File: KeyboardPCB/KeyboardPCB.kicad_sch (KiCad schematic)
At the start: 2 parts

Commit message: Equipment added
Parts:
- gave numbers to parts that had none: 2
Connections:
- net MCU_Battery/VBUSOUT is gone; now on net +5V: P1.A4 (VBUS), P1.A9 (VBUS), P1.B4 (VBUS), P1.B9 (VBUS)
- net MCU_Battery/VBUSIN renamed +5V

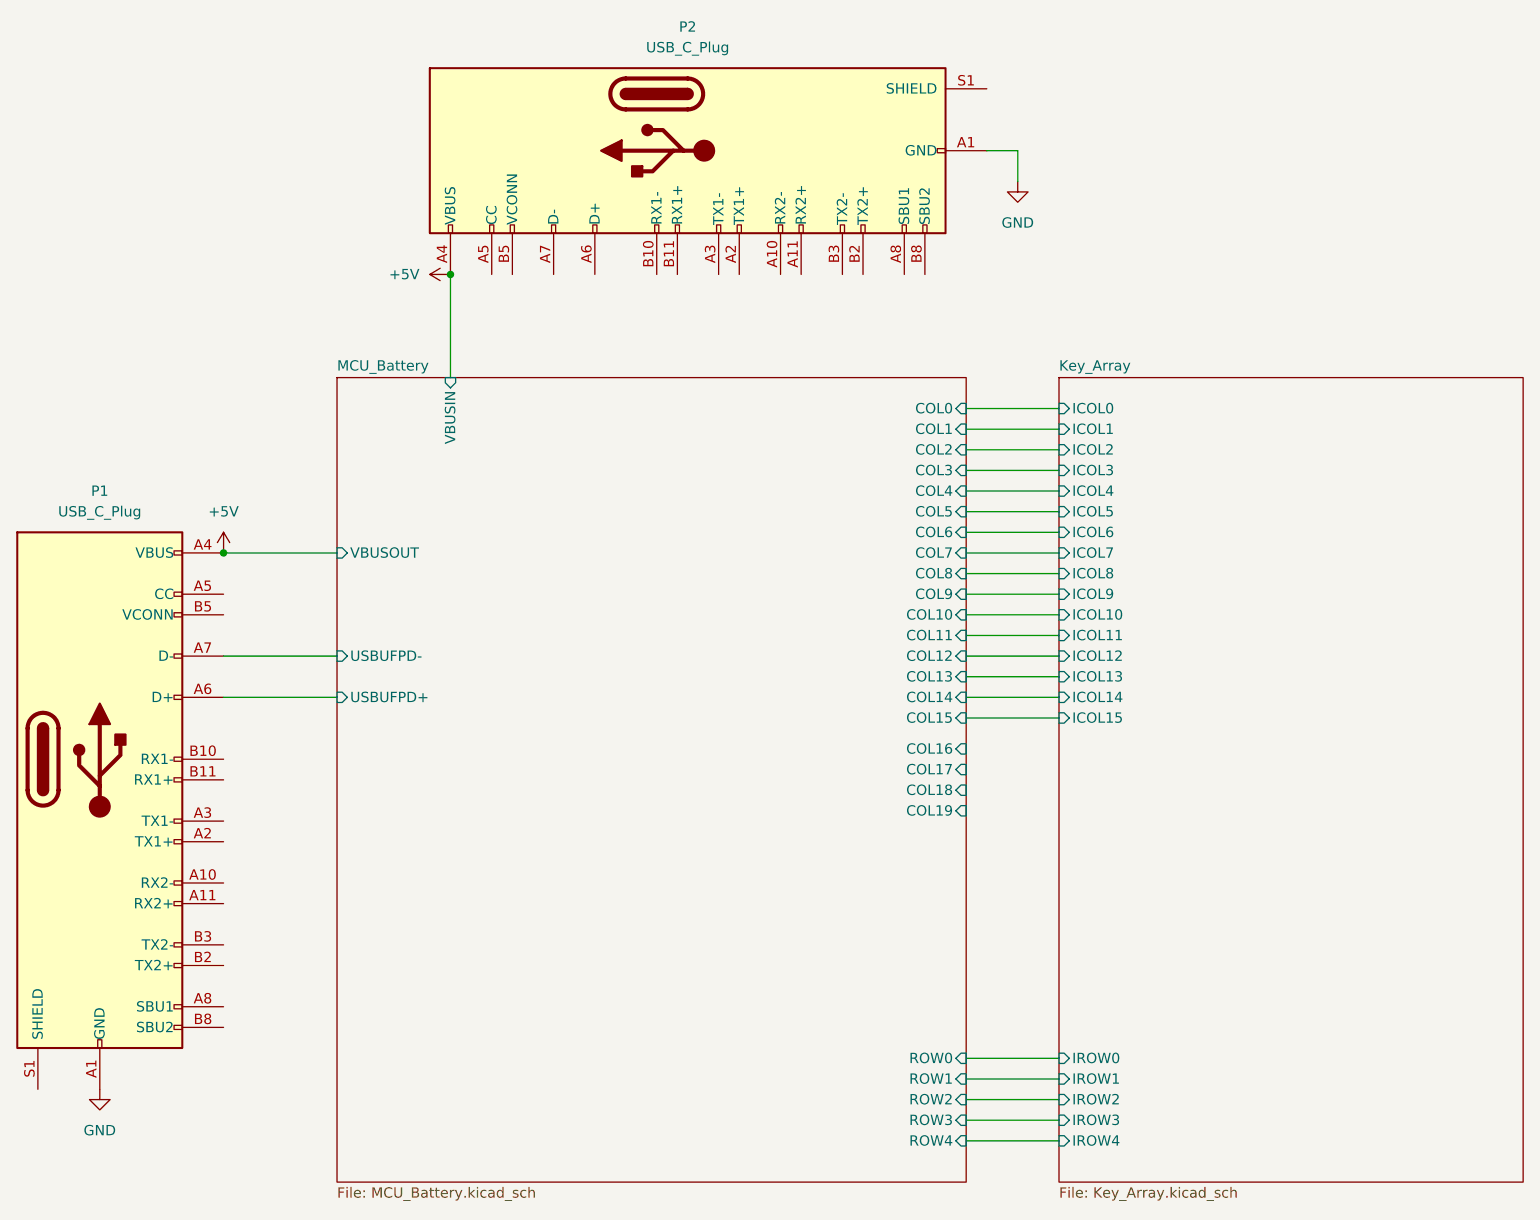
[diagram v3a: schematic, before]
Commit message: Added NCs
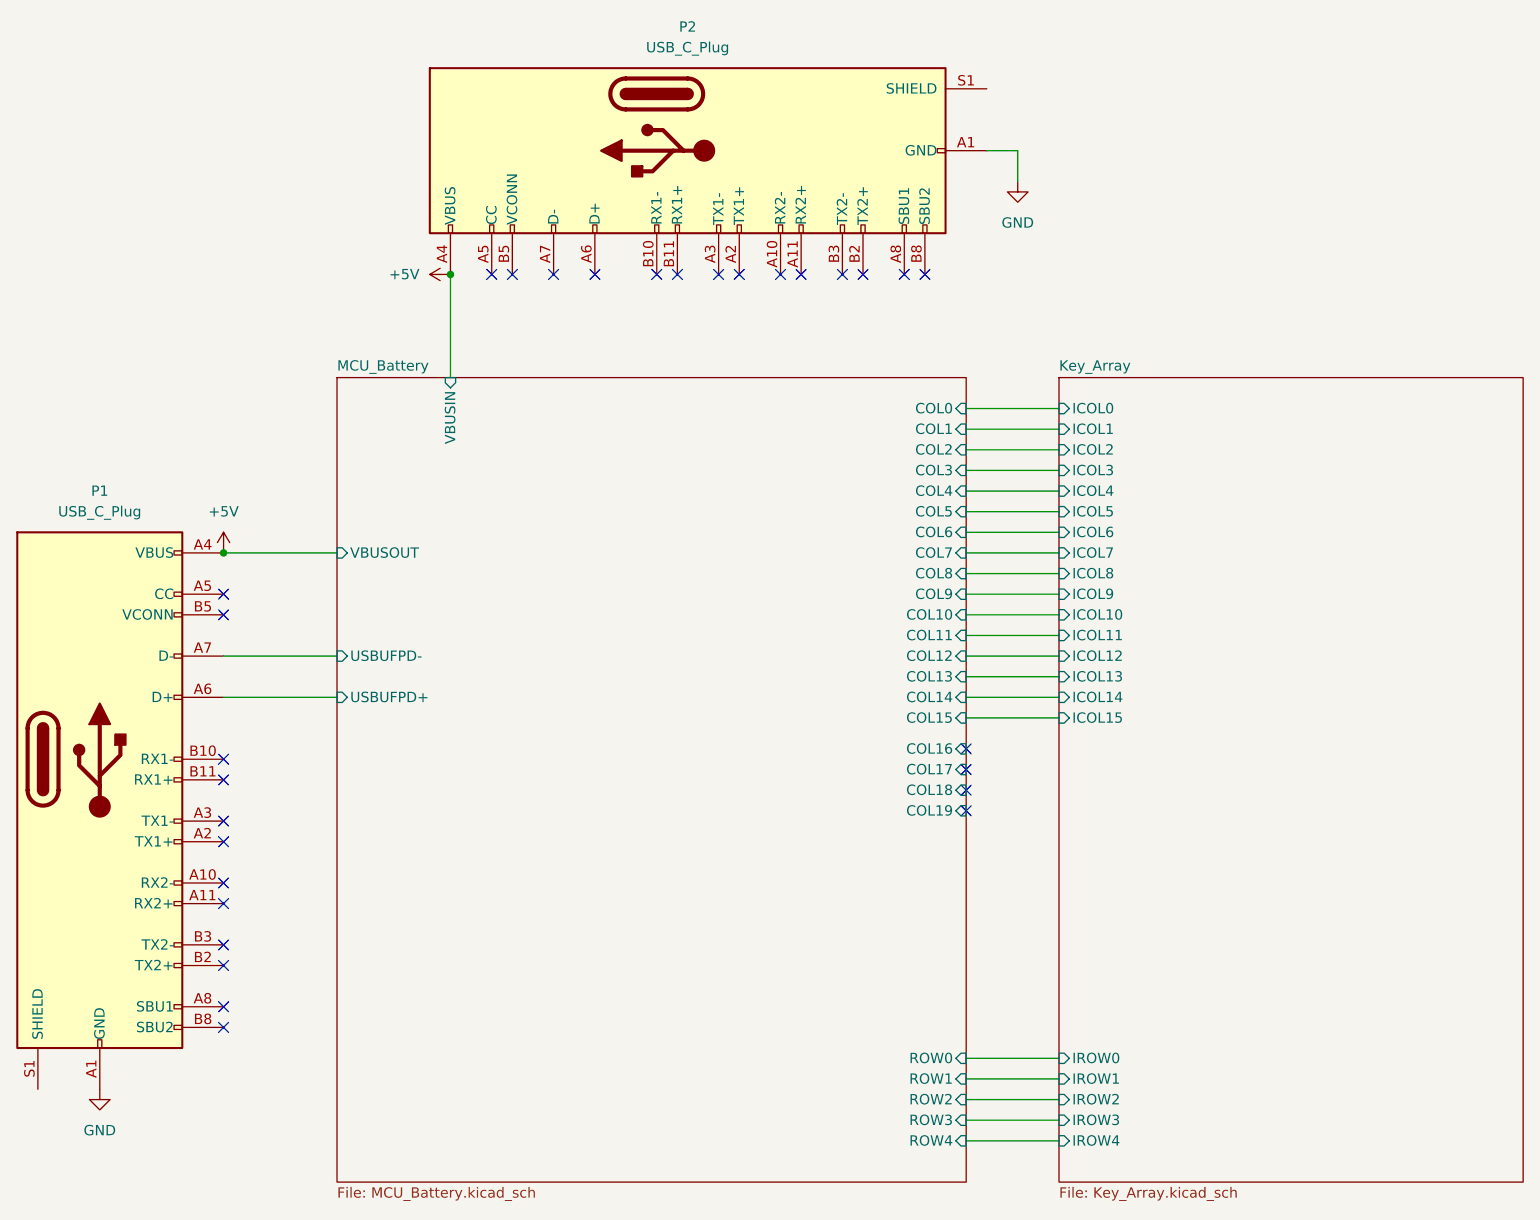
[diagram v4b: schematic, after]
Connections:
- no-connect marks 0 -> 30

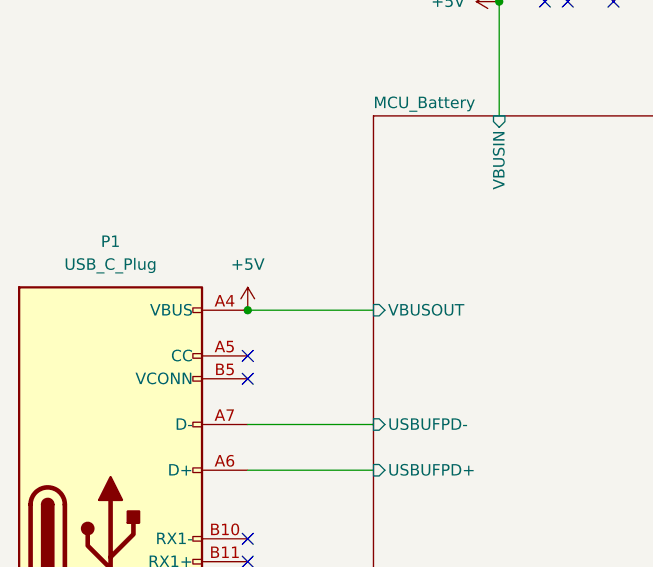
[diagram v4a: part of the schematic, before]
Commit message: added a 10k resistor
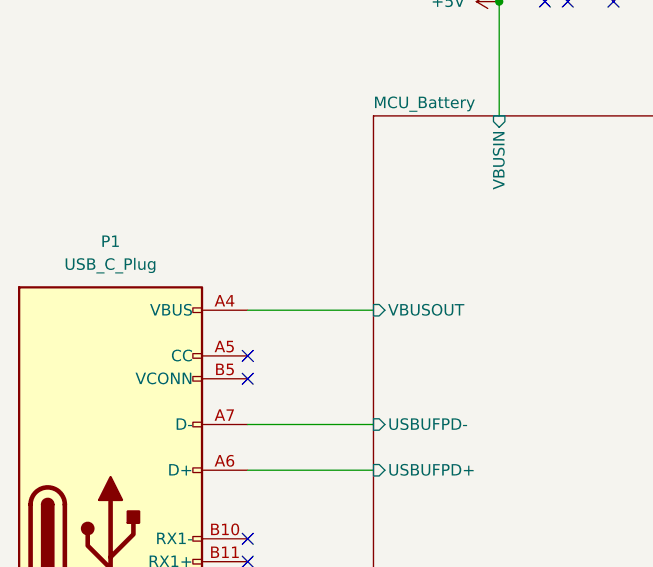
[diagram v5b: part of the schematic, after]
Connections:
- net +5V: no longer P1.A4 (VBUS), P1.A9 (VBUS), P1.B4 (VBUS), P1.B9 (VBUS)
- new net MCU_Battery/VBUSOUT: P1.A4 (VBUS), P1.A9 (VBUS), P1.B4 (VBUS), P1.B9 (VBUS)
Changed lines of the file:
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@@
   (junction (at 88.9 46.99) (diameter 0) (color 0 0 0 0)
-  )
-  (junction (at 60.96 81.28) (diameter 0) (color 0 0 0 0)
   )
   (no_connect (at 124.46 46.99))
@@
     (pin "S1")
   )
-  (symbol (lib_id "power:+5V") (at 60.96 81.28 0) (unit 1)
-    (in_bom yes) (on_board yes) (fields_autoplaced)
-    (property "Reference" "#PWR02" (id 0) (at 60.96 85.09 0)
-      (effects (font (size 1.27 1.27)) hide)
-    )
-    (property "Value" "+5V" (id 1) (at 60.96 76.2 0))
-    (property "Footprint" "" (id 2) (at 60.96 81.28 0)
-      (effects (font (size 1.27 1.27)) hide)
-    )
-    (property "Datasheet" "" (id 3) (at 60.96 81.28 0)
-      (effects (font (size 1.27 1.27)) hide)
-    )
-    (pin "1")
-  )
   (symbol (lib_id "power:GND") (at 45.72 147.32 0) (unit 1)
     (in_bom yes) (on_board yes) (fields_autoplaced)
@@
       (reference "#PWR01") (unit 1) (value "GND") (footprint "")
     )
-    (path "/12b6b2b1-fe05-4fac-93d7-1710e103d49c"
-      (reference "#PWR02") (unit 1) (value "+5V") (footprint "")
-    )
     (path "/6fb4039a-73ff-4aaa-834e-e47a8fd86b36"
       (reference "#PWR03") (unit 1) (value "+5V") (footprint "")
@@
       (reference "R2") (unit 1) (value "R") (footprint "")
     )
-    (path "/0e04ce72-6533-49cc-b4b5-6fa7ba1a6887/cd227165-3689-448f-a393-b1377c88e7b2"
+    (path "/0e04ce72-6533-49cc-b4b5-6fa7ba1a6887/f43f09d1-a598-404e-abc7-5bb9fdcb8a91"
       (reference "R3") (unit 1) (value "CRMA1206AF10K0DKEF") (footprint "RESC3216X74N")
     )
@@
       (reference "R4") (unit 1) (value "CRMA1206AF10K0DKEF") (footprint "RESC3216X74N")
     )
-    (path "/0e04ce72-6533-49cc-b4b5-6fa7ba1a6887/c2301fc4-e275-4763-8e5b-983bf1f23ff2"
-      (reference "R5") (unit 1) (value "R") (footprint "")
+    (path "/0e04ce72-6533-49cc-b4b5-6fa7ba1a6887/be295a14-ceda-4757-b5c9-058286067067"
+      (reference "R5") (unit 1) (value "CRMA1206AF10K0DKEF") (footprint "RESC3216X74N")
     )
     (path "/0e04ce72-6533-49cc-b4b5-6fa7ba1a6887/035328f6-5823-48a6-9a80-044707bde27e"
